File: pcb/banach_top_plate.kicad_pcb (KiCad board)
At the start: 2 copper layers, 129.6 x 90.7 mm, 27 parts, among them SW5 SW_PUSH

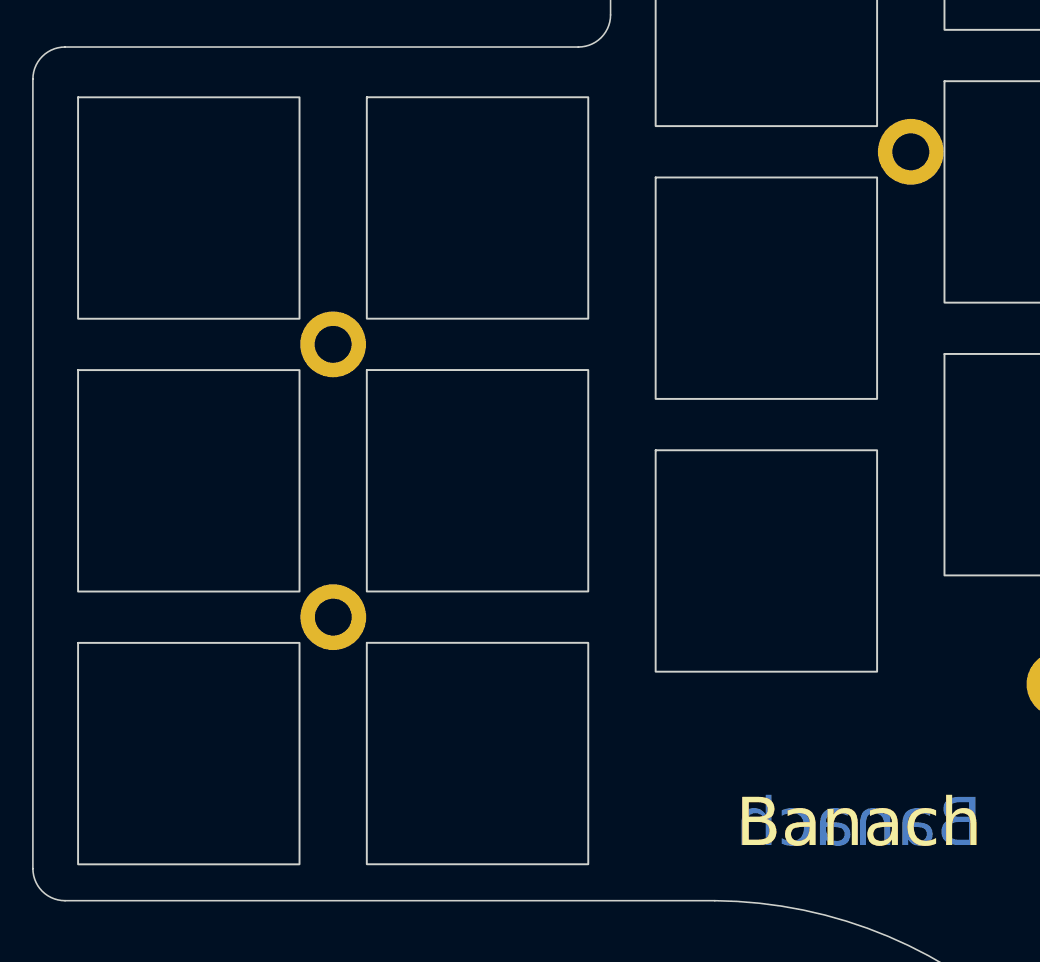
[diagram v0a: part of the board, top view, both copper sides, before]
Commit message: aligned column 0 to true choc spacing
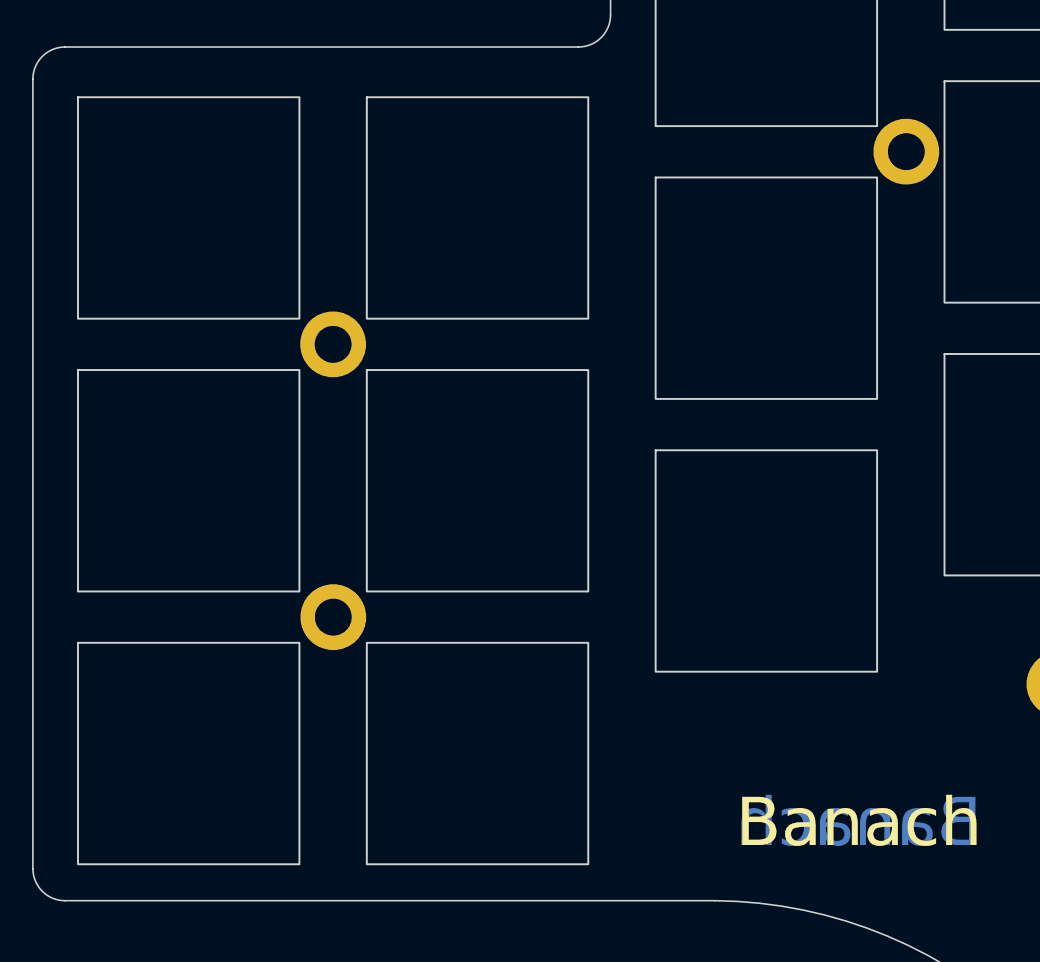
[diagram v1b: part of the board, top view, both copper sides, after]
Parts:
- moved h6 0.28 mm to (112.6, 66.9)
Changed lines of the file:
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@@
   )
   (footprint "kbd:SW_Hole_choc" (layer "F.Cu")
-    (at 67.916 70.404)
+    (at 67.91 70.4)
     (fp_text reference "SW5" (at 7 8.1) (layer "F.SilkS") hide
       (effects (font (size 1 1) (thickness 0.15)))
@@
   )
   (footprint "kbd:SW_Hole_choc" (layer "F.Cu")
-    (at 67.916 87.404)
+    (at 67.91 87.4)
     (fp_text reference "SW5" (at 7 8.1) (layer "F.SilkS") hide
       (effects (font (size 1 1) (thickness 0.15)))
@@
   )
   (footprint "kbd:SW_Hole_choc" (layer "F.Cu")
-    (at 67.916 104.404)
+    (at 67.91 104.4)
     (fp_text reference "SW5" (at 7 8.1) (layer "F.SilkS") hide
       (effects (font (size 1 1) (thickness 0.15)))
@@
   )
   (footprint "kbd:M2_Threads_v2" (layer "F.Cu")
-    (at 112.91 66.9)
+    (at 112.63 66.89)
     (descr "Mounting Hole 2.2mm, no annular, M2")
     (tags "mounting hole 2.2mm no annular m2")
